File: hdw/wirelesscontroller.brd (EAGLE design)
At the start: 99.1 x 55.9 mm, 18 parts

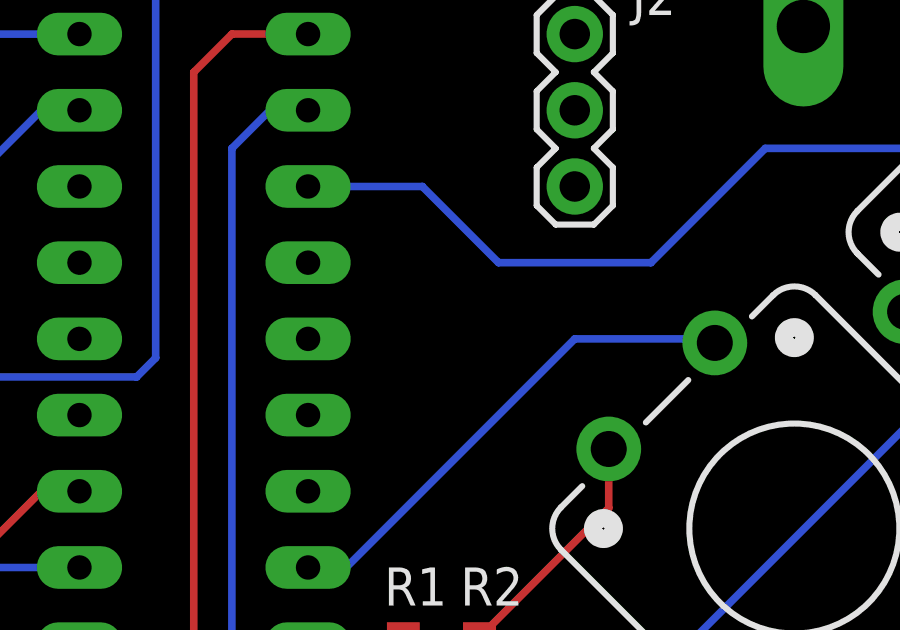
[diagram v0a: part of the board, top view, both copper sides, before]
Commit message: Added bypass cap
Added a bypass capacitor to the power supply on the controller
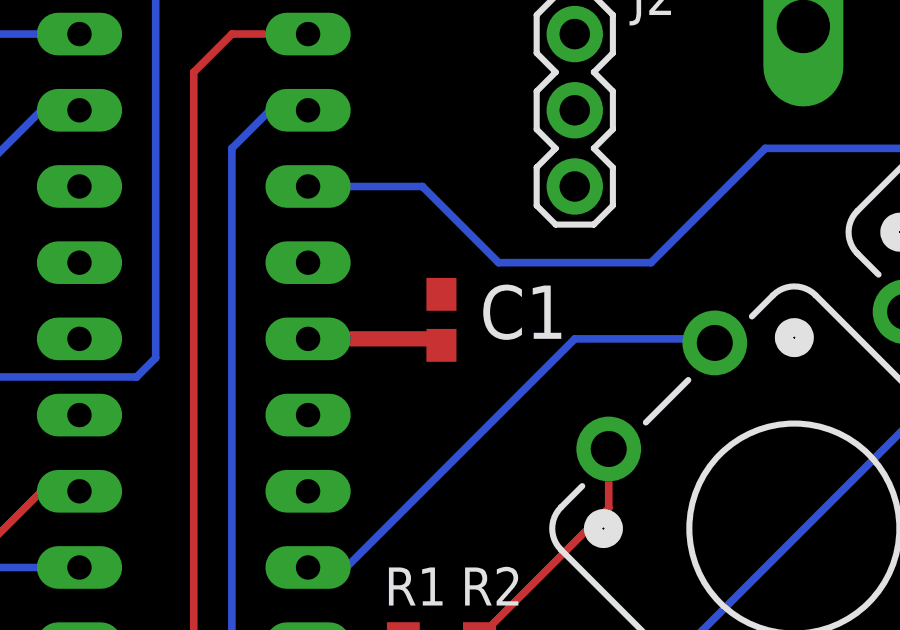
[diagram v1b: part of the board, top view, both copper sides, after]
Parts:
- added C1: 0.1uF, SparkFun-Capacitors:0603-CAP
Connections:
- net GND: now also C1.2
- net VCC: now also C1.1
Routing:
- net GND: track 37.6 -> 42.2 mm
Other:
- board text added: "C1"
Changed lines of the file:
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@@
 <text x="24.13" y="48.895" size="1.27" layer="22" rot="MR0">U4</text>
 <text x="76.835" y="48.895" size="1.27" layer="22" rot="MR0">U5</text>
+<text x="59.055" y="34.29" size="1.778" layer="21">C1</text>
 </plain>
 <attributes>
@@
 <element name="U$5" library="battery" package="AACLIP" value="AA_CUSTOM" x="69.85" y="27.94" rot="MR270"/>
 <element name="D$1" library="battery" package="R0603" value="DIODE" x="33.02" y="41.275" rot="R90"/>
+<element name="C1" library="SparkFun-Capacitors" package="0603-CAP" value="0.1uF" x="57.785" y="34.925" smashed="yes" rot="R270">
+<attribute name="PROD_ID" value="CAP-00810" x="57.785" y="34.925" size="1.778" layer="27" rot="R270" display="off"/>
+</element>
 </elements>
 <signals>
@@
 <wire x1="38.1" y1="19.05" x2="39.37" y2="17.78" width="0.254" layer="1"/>
 <wire x1="39.37" y1="17.78" x2="39.37" y2="13.97" width="0.4064" layer="1"/>
+<contactref element="C1" pad="1"/>
 </signal>
 <signal name="MOSI">
@@
 <wire x1="59.055" y1="24.345" x2="63.3621375" y2="28.6521375" width="0.254" layer="1"/>
 <wire x1="63.3621375" y1="28.6521375" x2="63.3621375" y2="30.619365625" width="0.254" layer="1"/>
+<contactref element="C1" pad="2"/>
+<wire x1="53.34" y1="34.29" x2="57.785" y2="34.29" width="0.508" layer="1"/>
+<wire x1="57.785" y1="34.29" x2="57.785" y2="34.075" width="0.4064" layer="1"/>
 </signal>
 <signal name="B1">
